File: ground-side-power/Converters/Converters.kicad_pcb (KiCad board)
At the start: 2 copper layers, 82.8 x 74.4 mm, 51 parts, among them J1 DAQ Voltage Sensing, J2 DAQ Current Sensing, J3 Ground Connections, J4 BATT_IN, J5 POWER_OUT, J6 5V_IN, U1 K7805-3AR3, U2 TPS55340, U3 INA180, U4 INA180

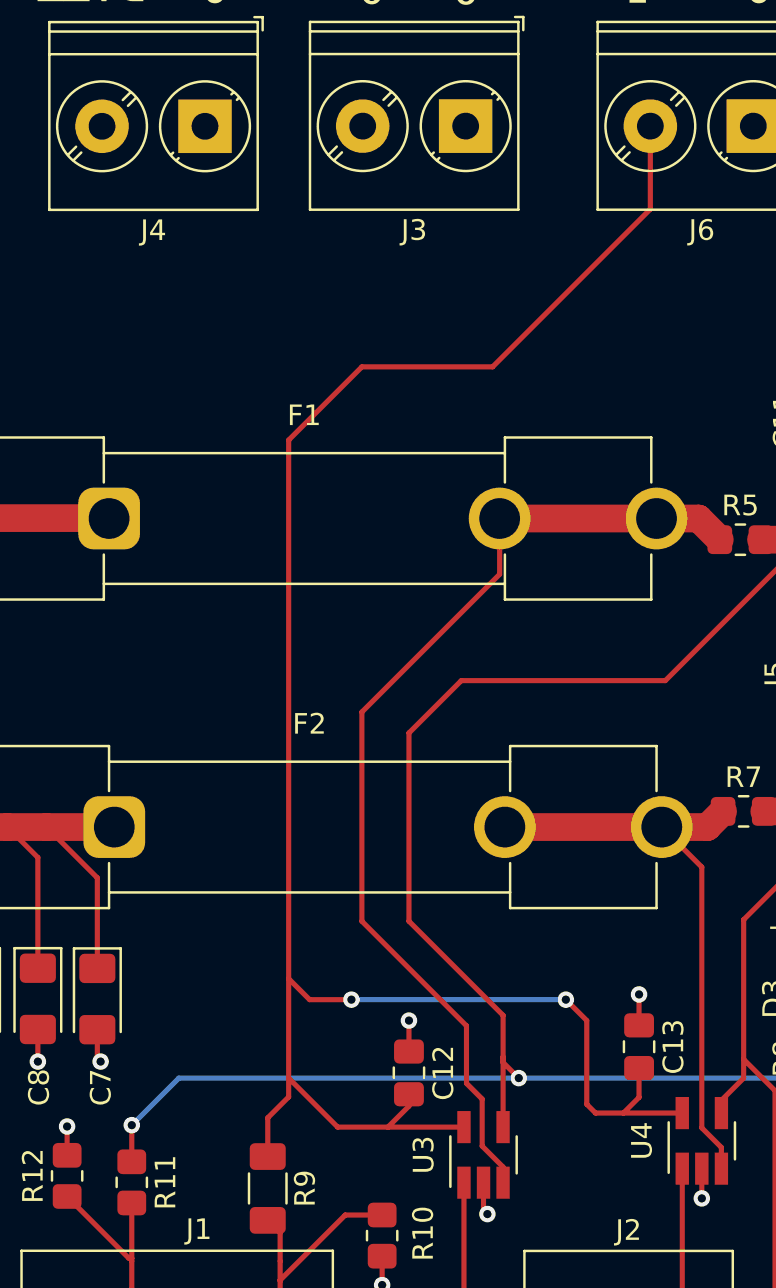
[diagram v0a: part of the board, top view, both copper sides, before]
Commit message: stitched 5v line
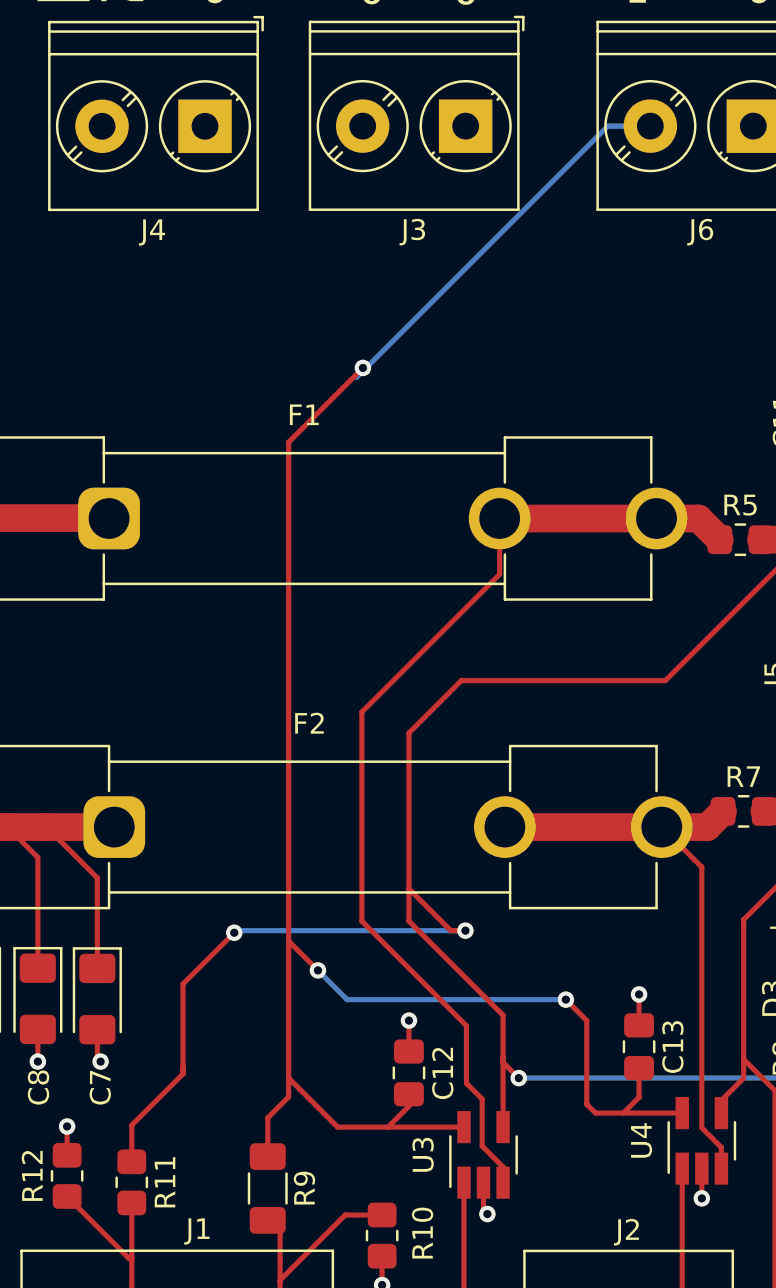
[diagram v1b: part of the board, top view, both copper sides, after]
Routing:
- net +5V: track 206.1 -> 212.1 mm, vias 4 -> 6
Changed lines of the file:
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@@
   (segment (start 166.878 121.685923) (end 166.116 122.447923) (width 0.25) (layer "F.Cu") (net 2))
   (segment (start 161.036 120.749923) (end 160.274 119.987923) (width 0.25) (layer "F.Cu") (net 2))
-  (segment (start 153.416 86.205923) (end 149.86 89.761923) (width 0.25) (layer "F.Cu") (net 2))
+  (segment (start 144.7292 116.1796) (end 144.7292 120.546723) (width 0.25) (layer "F.Cu") (net 2))
+  (segment (start 155.702 113.129923) (end 155.702 111.5568) (width 0.25) (layer "F.Cu") (net 2))
   (segment (start 152.24 123.129923) (end 154.686 123.129923) (width 0.25) (layer "F.Cu") (net 2))
   (segment (start 164.766 122.447923) (end 166.116 122.447923) (width 0.25) (layer "F.Cu") (net 2))
+  (segment (start 155.702 111.5568) (end 157.734 113.5888) (width 0.25) (layer "F.Cu") (net 2))
   (segment (start 168.154077 101.445923) (end 175 94.6) (width 0.25) (layer "F.Cu") (net 2))
   (segment (start 164.338 122.019923) (end 164.766 122.447923) (width 0.25) (layer "F.Cu") (net 2))
   (segment (start 179.9 90.8) (end 176.1 94.6) (width 0.25) (layer "F.Cu") (net 2))
+  (segment (start 160.274 117.701923) (end 156.160039 113.587961) (width 0.25) (layer "F.Cu") (net 2))
   (segment (start 155.702 122.113923) (end 154.686 123.129923) (width 0.25) (layer "F.Cu") (net 2))
-  (segment (start 167.426 74.513923) (end 167.426 78.545923) (width 0.25) (layer "F.Cu") (net 2))
-  (segment (start 159.766 86.205923) (end 153.416 86.205923) (width 0.25) (layer "F.Cu") (net 2))
+  (segment (start 149.86 89.8652) (end 153.4668 86.2584) (width 0.25) (layer "F.Cu") (net 2))
+  (segment (start 153.4668 86.2584) (end 153.416 86.205923) (width 0.25) (layer "F.Cu") (net 2))
+  (segment (start 144.7292 120.546723) (end 142.24 123.035923) (width 0.25) (layer "F.Cu") (net 2))
+  (segment (start 142.24 123.035923) (end 142.24 124.813923) (width 0.25) (layer "F.Cu") (net 2))
   (segment (start 175.6 89.9) (end 175.6 93) (width 0.25) (layer "F.Cu") (net 2))
-  (segment (start 149.86 115.923923) (end 150.876 116.939923) (width 0.25) (layer "F.Cu") (net 2))
-  (segment (start 142.24 124.813923) (end 142.24 123.035923) (width 0.25) (layer "F.Cu") (net 2))
+  (segment (start 157.734 113.5888) (end 158.4452 113.5888) (width 0.25) (layer "F.Cu") (net 2))
   (segment (start 158.242 101.445923) (end 168.154077 101.445923) (width 0.25) (layer "F.Cu") (net 2))
   (segment (start 155.702 103.985923) (end 158.242 101.445923) (width 0.25) (layer "F.Cu") (net 2))
@@
   (segment (start 148.844 122.682) (end 149.86 121.666) (width 0.25) (layer "F.Cu") (net 2))
   (segment (start 154.686 123.129923) (end 158.374 123.129923) (width 0.25) (layer "F.Cu") (net 2))
-  (segment (start 155.702 113.129923) (end 155.702 103.985923) (width 0.25) (layer "F.Cu") (net 2))
   (segment (start 179.9 89.107) (end 179.9 90.8) (width 0.25) (layer "F.Cu") (net 2))
-  (segment (start 167.426 78.545923) (end 159.766 86.205923) (width 0.25) (layer "F.Cu") (net 2))
+  (segment (start 151.2824 115.5192) (end 151.13 115.5192) (width 0.25) (layer "F.Cu") (net 2))
+  (segment (start 144.7292 120.1928) (end 144.7292 120.546723) (width 0.25) (layer "F.Cu") (net 2))
+  (segment (start 156.160039 113.587961) (end 155.702 113.129923) (width 0.25) (layer "F.Cu") (net 2))
   (segment (start 164.338 117.955923) (end 164.338 122.019923) (width 0.25) (layer "F.Cu") (net 2))
   (segment (start 148.844 124.559923) (end 148.844 122.682) (width 0.25) (layer "F.Cu") (net 2))
+  (segment (start 149.86 120.749923) (end 149.86 114.0968) (width 0.25) (layer "F.Cu") (net 2))
   (segment (start 172.8 94.6) (end 174 94.6) (width 1.3462) (layer "F.Cu") (net 2))
+  (segment (start 151.2824 115.5192) (end 149.86 114.0968) (width 0.25) (layer "F.Cu") (net 2))
+  (segment (start 147.2184 113.6904) (end 144.7292 116.1796) (width 0.25) (layer "F.Cu") (net 2))
   (segment (start 166.116 122.447923) (end 168.976 122.447923) (width 0.25) (layer "F.Cu") (net 2))
   (segment (start 177.050077 94.6) (end 178.562 96.111923) (width 1.3462) (layer "F.Cu") (net 2))
   (segment (start 149.86 121.666) (end 149.86 120.749923) (width 0.25) (layer "F.Cu") (net 2))
-  (segment (start 160.274 117.701923) (end 155.702 113.129923) (width 0.25) (layer "F.Cu") (net 2))
   (segment (start 166.878 120.263423) (end 166.878 121.685923) (width 0.25) (layer "F.Cu") (net 2))
   (segment (start 160.274 119.987923) (end 160.274 119.733923) (width 0.25) (layer "F.Cu") (net 2))
-  (segment (start 149.86 89.761923) (end 149.86 115.923923) (width 0.25) (layer "F.Cu") (net 2))
+  (segment (start 155.702 111.5568) (end 155.702 103.985923) (width 0.25) (layer "F.Cu") (net 2))
+  (segment (start 149.86 114.0968) (end 149.86 89.8652) (width 0.25) (layer "F.Cu") (net 2))
+  (segment (start 156.160878 113.5888) (end 156.160039 113.587961) (width 0.25) (layer "F.Cu") (net 2))
   (segment (start 163.322 116.939923) (end 164.338 117.955923) (width 0.25) (layer "F.Cu") (net 2))
-  (segment (start 149.86 115.923923) (end 149.86 120.749923) (width 0.25) (layer "F.Cu") (net 2))
   (segment (start 155.702 121.533423) (end 155.702 122.113923) (width 0.25) (layer "F.Cu") (net 2))
   (segment (start 160.274 123.129923) (end 160.274 119.733923) (width 0.25) (layer "F.Cu") (net 2))
@@
   (segment (start 176.1 94.6) (end 177.050077 94.6) (width 1.3462) (layer "F.Cu") (net 2))
   (segment (start 149.86 120.749923) (end 152.24 123.129923) (width 0.25) (layer "F.Cu") (net 2))
-  (segment (start 150.876 116.939923) (end 152.908 116.939923) (width 0.25) (layer "F.Cu") (net 2))
-  (via (at 152.908 116.939923) (size 0.8) (drill 0.4) (layers "F.Cu" "B.Cu") (free) (net 2))
+  (via (at 158.4452 113.5888) (size 0.8) (drill 0.4) (layers "F.Cu" "B.Cu") (free) (net 2))
+  (via (at 151.2824 115.5192) (size 0.8) (drill 0.4) (layers "F.Cu" "B.Cu") (free) (net 2))
   (via (at 163.322 116.939923) (size 0.8) (drill 0.4) (layers "F.Cu" "B.Cu") (free) (net 2))
   (via (at 161.036 120.749923) (size 0.8) (drill 0.4) (layers "F.Cu" "B.Cu") (net 2))
-  (via (at 142.24 123.035923) (size 0.8) (drill 0.4) (layers "F.Cu" "B.Cu") (free) (net 2))
-  (segment (start 161.036 120.749923) (end 144.526 120.749923) (width 0.25) (layer "B.Cu") (net 2))
-  (segment (start 152.908 116.939923) (end 163.322 116.939923) (width 0.25) (layer "B.Cu") (net 2))
+  (via (at 147.2184 113.6904) (size 0.8) (drill 0.4) (layers "F.Cu" "B.Cu") (free) (net 2))
+  (via (at 153.4668 86.2584) (size 0.8) (drill 0.4) (layers "F.Cu" "B.Cu") (net 2))
+  (segment (start 151.2824 115.5192) (end 152.703123 116.939923) (width 0.25) (layer "B.Cu") (net 2))
+  (segment (start 152.703123 116.939923) (end 163.322 116.939923) (width 0.25) (layer "B.Cu") (net 2))
+  (segment (start 167.426 74.513923) (end 165.363677 74.513923) (width 0.25) (layer "B.Cu") (net 2))
+  (segment (start 165.363677 74.513923) (end 153.162 86.7156) (width 0.25) (layer "B.Cu") (net 2))
+  (segment (start 147.32 113.5888) (end 147.2184 113.6904) (width 0.25) (layer "B.Cu") (net 2))
   (segment (start 161.036 120.749923) (end 180.950077 120.749923) (width 0.25) (layer "B.Cu") (net 2))
-  (segment (start 144.526 120.749923) (end 142.24 123.035923) (width 0.25) (layer "B.Cu") (net 2))
   (segment (start 180.950077 120.749923) (end 181.4 120.3) (width 0.25) (layer "B.Cu") (net 2))
+  (segment (start 158.4452 113.5888) (end 147.32 113.5888) (width 0.25) (layer "B.Cu") (net 2))
   (segment (start 115.1375 127.4) (end 115.1375 126.75) (width 0.4572) (layer "F.Cu") (net 3))
   (segment (start 115.1375 126.75) (end 112.575 126.75) (width 0.4572) (layer "F.Cu") (net 3))
